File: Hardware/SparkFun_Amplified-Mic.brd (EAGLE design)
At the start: 22.1 x 10.2 mm, 15 parts, among them M1 MIC9.7MM, U1 OPA344

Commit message: Ready for Review
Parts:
- M1: device SparkFun:MIC-9.7MM -> SparkFun-Sensors:MIC-9.7MM
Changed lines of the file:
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@@
 <layer number="113" name="IDFDebug" color="4" fill="1" visible="yes" active="yes"/>
 <layer number="116" name="Patch_BOT" color="9" fill="4" visible="yes" active="yes"/>
+<layer number="118" name="Rect_Pads" color="7" fill="1" visible="yes" active="yes"/>
 <layer number="121" name="_tsilk" color="7" fill="1" visible="yes" active="yes"/>
 <layer number="122" name="_bsilk" color="7" fill="1" visible="yes" active="yes"/>
@@
 </autorouter>
 <elements>
-<element name="M1" library="SparkFun" package="MIC-9.7MM" value="MIC9.7MM" x="5.08" y="5.08" rot="MR180"/>
+<element name="M1" library="SparkFun-Sensors" package="MIC-9.7MM" value="MIC9.7MM" x="5.08" y="5.08" rot="MR180">
+<attribute name="PROD_ID" value="COMP-08856" x="5.08" y="5.08" size="1.778" layer="28" rot="MR180" display="off"/>
+</element>
 <element name="U1" library="SparkFun" package="SOT23-5" value="OPA344" x="12.954" y="5.08" smashed="yes" rot="R90">
 <attribute name="NAME" x="10.795" y="4.191" size="0.4064" layer="25" rot="R90"/>

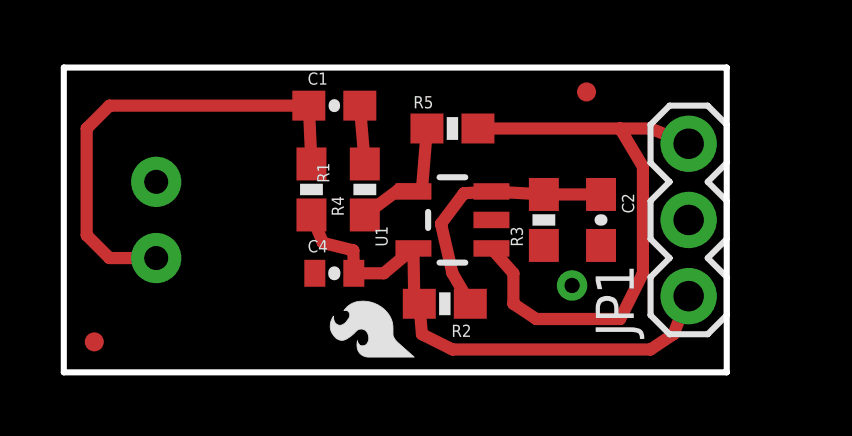
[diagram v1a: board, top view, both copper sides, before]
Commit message: Revised Board and Schematic per Design review 2/8/2016
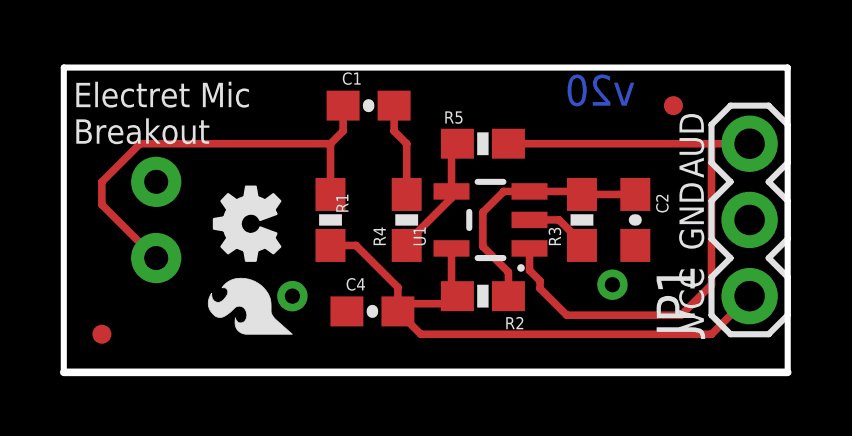
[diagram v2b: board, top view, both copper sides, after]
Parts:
- added LOGO1: OSHW-LOGOMINI, SparkFun-Aesthetics:OSHW-LOGO-MINI
- added U$2: REVISION, SparkFun-Aesthetics:REVISION
- C4: device SparkFun:0402-CAP -> SparkFun-Capacitors:0603-CAP
- U1: device SparkFun:SOT23-5 -> SparkFun-AnalogIC:SOT23-5
- moved U$1 4.13 mm to (7.62, 1.27)
- moved JP2 2.93 mm to (20.3, 8.89)
- moved JP1 2.03 mm to (22.9, 2.54)
- moved C4 1.80 mm to (10.3, 2.03)
- moved R4 1.73 mm to (11.4, 5.08)
- moved R2 1.30 mm to (14.0, 2.54)
- moved R3 1.27 mm to (17.3, 5.08)
- moved U1 1.27 mm to (14.2, 5.08)
- moved R1 1.20 mm to (8.89, 5.08)
- moved C1 1.14 mm to (10.2, 8.89)
- moved C2 1.14 mm to (19.1, 5.08)
- moved R5 1.14 mm to (14.0, 7.62)
- moved JP3 0.36 mm to (1.27, 1.27)
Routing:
- net GND: track 0.00 -> 2.44 mm, vias 1 -> 2
- net VCC: track 18.2 -> 20.1 mm
- net N$1: track 15.9 -> 14.6 mm
- net N$6: track 1.95 -> 3.13 mm
- net AUD: track 19.7 -> 20.7 mm
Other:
- board size 22.1 x 10.2 mm -> 24.1 x 10.2 mm
- board text added: "All units inches"
- board text added: "Electret Mic Breakout"
- board text added: "Mary E West"
- board text added: "v20"
- board text removed: "Mic Breakout"

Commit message: Updated Board and Schematic files. Added product ID to Res5 and removed 10mils of board
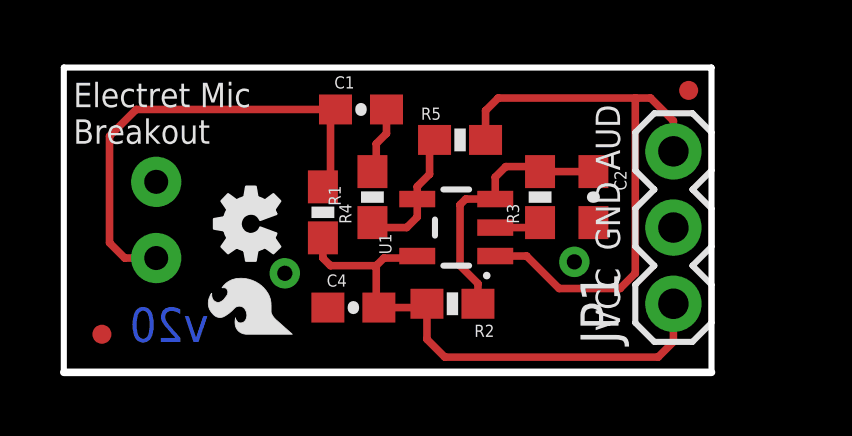
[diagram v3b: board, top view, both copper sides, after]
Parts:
- moved JP1 2.55 mm to (20.3, 2.29)
- moved C2 1.59 mm to (17.7, 5.84)
- moved R3 1.59 mm to (15.9, 5.84)
- moved R4 1.37 mm to (10.3, 5.84)
- moved U1 1.17 mm to (13.1, 4.83)
- moved R2 1.05 mm to (13.0, 2.29)
- moved R5 0.77 mm to (13.2, 7.75)
- moved JP2 0.72 mm to (20.8, 9.40)
- moved C4 0.65 mm to (9.65, 2.16)
- moved R1 0.36 mm to (8.64, 5.33)
- moved C1 0.28 mm to (9.91, 8.76)
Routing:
- net VCC: track 20.1 -> 18.3 mm
- net N$1: track 14.6 -> 16.0 mm
- net GND: track 2.44 -> 1.56 mm
- net N$6: track 3.13 -> 2.27 mm
- net AUD: track 20.7 -> 19.9 mm
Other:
- board size 24.1 x 10.2 mm -> 21.6 x 10.2 mm
